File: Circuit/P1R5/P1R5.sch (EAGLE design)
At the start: 181 parts, among them J1 2X5_0.05"_CORTEX_DEBUGTH_NOKE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, U1 MK20DX256VLH7, U2 TPS61200, U3 PCA9552BS, U4 PCA9552BS, U5 MPU-9250, U6 ESP8266EX, U7 25Q40, U8 NRF24L01, Y1 8MHz, Y2 34.728kHz, Y3 26 Mhz, Y4 16 Mhz

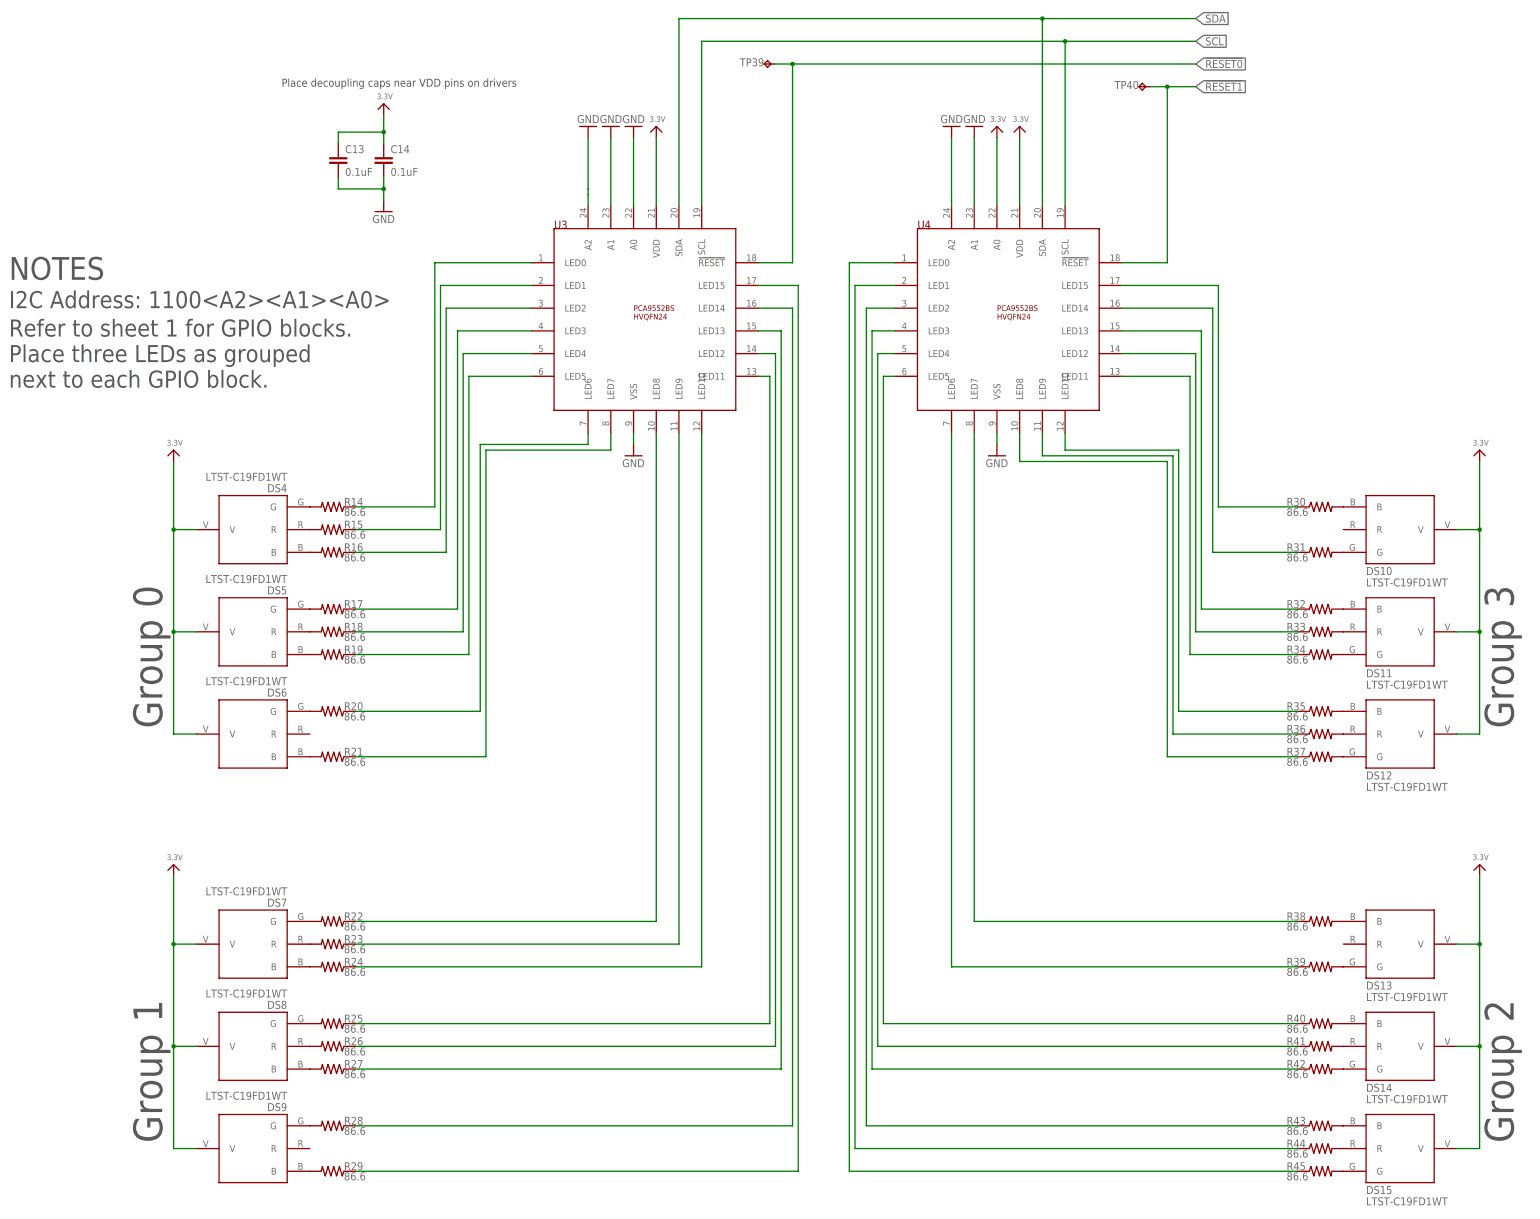
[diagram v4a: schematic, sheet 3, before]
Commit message: Everything but 3 banks of LED's is routed.
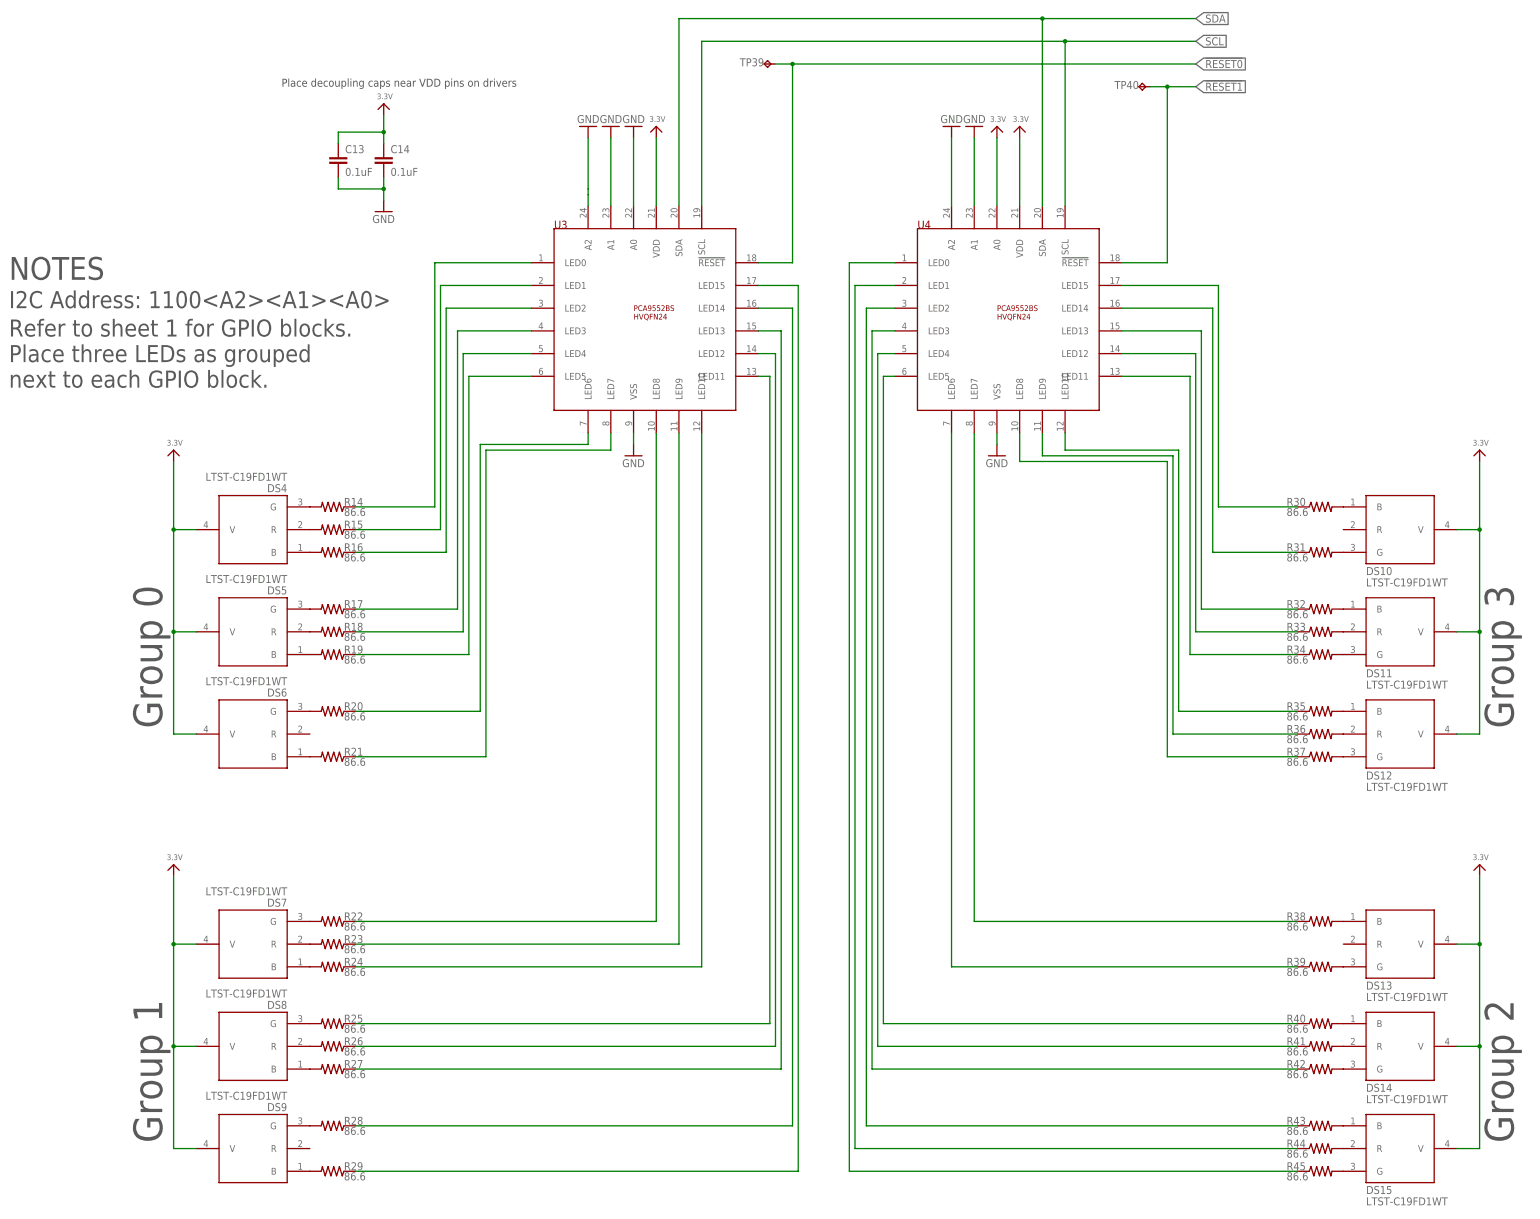
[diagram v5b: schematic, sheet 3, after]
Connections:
- net !RESET0: now also U1.PTC11/ADC1_SE7B; no longer U1.PTC10/ADC1_SE6B
- net FSYNC: now also U1.PTC10/ADC1_SE6B; no longer U1.PTC11/ADC1_SE7B
- net N$10: now also U1.PTD5/SPI0_PCS2; no longer U1.PTD0/SPI0_PCS0
- net N$16: now also U1.PTD0/SPI0_PCS0; no longer U1.PTD5/SPI0_PCS2
- net N$20: now also TP19.TP; no longer TP20.TP
- net N$21: now also TP20.TP; no longer TP19.TP
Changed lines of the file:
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@@
 <pinref part="DS1" gate="G$1" pin="C"/>
 <wire x1="236.22" y1="-77.47" x2="236.22" y2="-74.93" width="0.1524" layer="91"/>
-<pinref part="U1" gate="G$1" pin="PTD0/SPI0_PCS0"/>
+<pinref part="U1" gate="G$1" pin="PTD5/SPI0_PCS2"/>
 <wire x1="201.93" y1="-77.47" x2="236.22" y2="-77.47" width="0.1524" layer="91"/>
 </segment>
@@
 <wire x1="217.17" y1="-139.7" x2="217.17" y2="-143.51" width="0.1524" layer="91"/>
 <label x="295.91" y="-156.21" size="1.778" layer="95" xref="yes"/>
-<pinref part="U1" gate="G$1" pin="PTC11/ADC1_SE7B"/>
+<pinref part="U1" gate="G$1" pin="PTC10/ADC1_SE6B"/>
 <wire x1="201.93" y1="-143.51" x2="217.17" y2="-143.51" width="0.1524" layer="91"/>
 </segment>
@@
 </segment>
 </net>
-<net name="N$20" class="0">
-<segment>
-<pinref part="U1" gate="G$1" pin="PTA13/CAN0_RX"/>
-<pinref part="TP20" gate="G$1" pin="TP"/>
-<wire x1="201.93" y1="-201.93" x2="222.25" y2="-201.93" width="0.1524" layer="91"/>
-</segment>
-</net>
-<net name="N$21" class="0">
-<segment>
-<pinref part="TP19" gate="G$1" pin="TP"/>
-<pinref part="U1" gate="G$1" pin="PTA12/CAN0_TX"/>
-<wire x1="222.25" y1="-199.39" x2="201.93" y2="-199.39" width="0.1524" layer="91"/>
-</segment>
-</net>
 <net name="!RESET0" class="0">
 <segment>
 <wire x1="201.93" y1="-176.53" x2="295.91" y2="-176.53" width="0.1524" layer="91"/>
 <label x="295.91" y="-176.53" size="1.778" layer="95" xref="yes"/>
-<pinref part="U1" gate="G$1" pin="PTC10/ADC1_SE6B"/>
+<pinref part="U1" gate="G$1" pin="PTC11/ADC1_SE7B"/>
 </segment>
 </net>
 <net name="!RESET1" class="0">
 <segment>
-<pinref part="U1" gate="G$1" pin="PTA5"/>
-<wire x1="201.93" y1="-179.07" x2="246.38" y2="-179.07" width="0.1524" layer="91"/>
 <wire x1="246.38" y1="-179.07" x2="246.38" y2="-180.34" width="0.1524" layer="91"/>
 <wire x1="246.38" y1="-180.34" x2="295.91" y2="-180.34" width="0.1524" layer="91"/>
 <label x="295.91" y="-180.34" size="1.778" layer="95" xref="yes"/>
+<pinref part="U1" gate="G$1" pin="PTA5"/>
+<wire x1="201.93" y1="-179.07" x2="246.38" y2="-179.07" width="0.1524" layer="91"/>
 </segment>
 </net>
@@
 </segment>
 </net>
-<net name="N$16" class="0">
-<segment>
-<pinref part="U1" gate="G$1" pin="PTD5/SPI0_PCS2"/>
-<pinref part="TP24" gate="G$1" pin="TP"/>
-<wire x1="201.93" y1="-214.63" x2="222.25" y2="-214.63" width="0.1524" layer="91"/>
-</segment>
-</net>
 <net name="N$17" class="0">
 <segment>
@@
 </segment>
 </net>
+<net name="N$16" class="0">
+<segment>
+<pinref part="U1" gate="G$1" pin="PTD0/SPI0_PCS0"/>
+<pinref part="TP24" gate="G$1" pin="TP"/>
+<wire x1="201.93" y1="-214.63" x2="222.25" y2="-214.63" width="0.1524" layer="91"/>
+</segment>
+</net>
+<net name="N$20" class="0">
+<segment>
+<pinref part="U1" gate="G$1" pin="PTA13/CAN0_RX"/>
+<pinref part="TP19" gate="G$1" pin="TP"/>
+<wire x1="201.93" y1="-199.39" x2="222.25" y2="-199.39" width="0.1524" layer="91"/>
+</segment>
+</net>
+<net name="N$21" class="0">
+<segment>
+<pinref part="U1" gate="G$1" pin="PTA12/CAN0_TX"/>
+<pinref part="TP20" gate="G$1" pin="TP"/>
+<wire x1="201.93" y1="-201.93" x2="222.25" y2="-201.93" width="0.1524" layer="91"/>
+</segment>
+</net>

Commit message: Finished routing PCB. Put on some labels.
DOPE
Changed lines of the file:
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@@
 <setting verticaltext="up"/>
 </settings>
-<grid distance="0.05" unitdist="inch" unit="inch" style="lines" multiple="1" display="no" altdistance="0.01" altunitdist="inch" altunit="inch"/>
+<grid distance="0.1" unitdist="inch" unit="inch" style="lines" multiple="1" display="no" altdistance="0.01" altunitdist="inch" altunit="inch"/>
 <layers>
 <layer number="1" name="Top" color="4" fill="1" visible="no" active="no"/>
@@
 any power source where 2.5 &lt; Vout &lt; 7v
 See sheet 2 for regulator circuit.</text>
-<text x="110.49" y="-90.17" size="1.778" layer="97">Place decoupling caps near power pins.</text>
+<text x="52.07" y="-82.55" size="1.778" layer="97">Place decoupling caps near power pins.</text>
 <text x="140.97" y="-254" size="1.778" layer="97">0: X- Group</text>
 <text x="200.66" y="-254" size="1.778" layer="97">2: Y+ Group</text>
